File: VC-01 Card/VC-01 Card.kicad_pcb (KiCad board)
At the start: 2 copper layers, 55 x 41 mm, 60 parts, among them J1 AudioJack3, J2 Jack-DC, U1 ADS8681RUM, U2 TPS7A8801RTJT, U3 ADS8681RUM, U4 W25Q32JVSS, U5 LM1117-ADJ

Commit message: Added burden resistor jumper
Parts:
- added J3: BRDN, Connector_PinHeader_2.54mm:PinHeader_1x02_P2.54mm_Vertical, F.Cu at (150.7, 100.2)
- R1: footprint Resistor_SMD:R_2512_6332Metric -> Resistor_SMD:R_0805_2012Metric
- moved R1 10.8 mm to (144.8, 100.1), turned to 270 degrees
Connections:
- R1 pad 1: Net-(C2-Pad2) -> Net-(J3-Pad2)
- R1 pad 2: Net-(C2-Pad1) -> Net-(C2-Pad2)
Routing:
- net Net-(C2-Pad1): track 14.7 -> 7.66 mm
- net Net-(C2-Pad2): track 8.01 -> 13.4 mm
- net Net-(J3-Pad2): track 0.00 -> 3.79 mm
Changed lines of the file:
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@@
     (thickness 1.6)
     (drawings 55)
-    (tracks 497)
+    (tracks 498)
     (zones 0)
-    (modules 60)
-    (nets 41)
+    (modules 61)
+    (nets 42)
   )
   (page A4)
@@
   (net 39 /U1_GNDA)
   (net 40 /U3_GNDA)
+  (net 41 "Net-(J3-Pad2)")
   (net_class Default "This is the default net class."
     (clearance 0.2)
@@
     (add_net "Net-(J2-Pad1)")
     (add_net "Net-(J2-Pad2)")
+    (add_net "Net-(J3-Pad2)")
   )
   (net_class "Analog Path IC" ""
@@
     )
   )
-  (module Resistor_SMD:R_2512_6332Metric (layer F.Cu)
-    (at 147 110.7 180)
-    (descr "Resistor SMD 2512 (6332 Metric), square (rectangular) end terminal, IPC_7351 nominal, (Body size source: http://www.tortai-tech.com/upload/download/2011102023233369053.pdf), generated with kicad-footprint-generator")
-    (tags resistor)
-    (attr smd)
-    (fp_text reference R1 (at 0 -2.62) (layer F.SilkS)
-      (effects (font (size 1 1) (thickness 0.15)))
-    )
-    (fp_text value RB (at 0 2.62) (layer F.Fab)
-      (effects (font (size 1 1) (thickness 0.15)))
-    )
-    (fp_line (start -3.15 1.6) (end -3.15 -1.6) (layer F.Fab) (width 0.1))
-    (fp_line (start -3.15 -1.6) (end 3.15 -1.6) (layer F.Fab) (width 0.1))
-    (fp_line (start 3.15 -1.6) (end 3.15 1.6) (layer F.Fab) (width 0.1))
-    (fp_line (start 3.15 1.6) (end -3.15 1.6) (layer F.Fab) (width 0.1))
-    (fp_line (start -2.052064 -1.71) (end 2.052064 -1.71) (layer F.SilkS) (width 0.12))
-    (fp_line (start -2.052064 1.71) (end 2.052064 1.71) (layer F.SilkS) (width 0.12))
-    (fp_line (start -3.82 1.92) (end -3.82 -1.92) (layer F.CrtYd) (width 0.05))
-    (fp_line (start -3.82 -1.92) (end 3.82 -1.92) (layer F.CrtYd) (width 0.05))
-    (fp_line (start 3.82 -1.92) (end 3.82 1.92) (layer F.CrtYd) (width 0.05))
-    (fp_line (start 3.82 1.92) (end -3.82 1.92) (layer F.CrtYd) (width 0.05))
-    (fp_text user %R (at 0 0) (layer F.Fab)
-      (effects (font (size 1 1) (thickness 0.15)))
-    )
-    (pad 1 smd roundrect (at -2.9 0 180) (size 1.35 3.35) (layers F.Cu F.Paste F.Mask) (roundrect_rratio 0.185185)
-      (net 7 "Net-(C2-Pad2)"))
-    (pad 2 smd roundrect (at 2.9 0 180) (size 1.35 3.35) (layers F.Cu F.Paste F.Mask) (roundrect_rratio 0.185185)
-      (net 6 "Net-(C2-Pad1)"))
-    (model ${KISYS3DMOD}/Resistor_SMD.3dshapes/R_2512_6332Metric.wrl
-      (at (xyz 0 0 0))
-      (scale (xyz 1 1 1))
-      (rotate (xyz 0 0 0))
-    )
-  )
   (module Resistor_SMD:R_0603_1608Metric (layer F.Cu)
     (at 164.6 100.4)
@@
     )
   )
+  (module Resistor_SMD:R_0805_2012Metric (layer F.Cu)
+    (at 144.8 100.1 270)
+    (descr "Resistor SMD 0805 (2012 Metric), square (rectangular) end terminal, IPC_7351 nominal, (Body size source: https://docs.google.com/spreadsheets/d/1BsfQQcO9C6DZCsRaXUlFlo91Tg2WpOkGARC1WS5S8t0/edit?usp=sharing), generated with kicad-footprint-generator")
+    (tags resistor)
+    (attr smd)
+    (fp_text reference R1 (at 0 -1.65 90) (layer F.SilkS)
+      (effects (font (size 1 1) (thickness 0.15)))
+    )
+    (fp_text value RB (at 0 1.65 90) (layer F.Fab)
+      (effects (font (size 1 1) (thickness 0.15)))
+    )
+    (fp_line (start -1 0.6) (end -1 -0.6) (layer F.Fab) (width 0.1))
+    (fp_line (start -1 -0.6) (end 1 -0.6) (layer F.Fab) (width 0.1))
+    (fp_line (start 1 -0.6) (end 1 0.6) (layer F.Fab) (width 0.1))
+    (fp_line (start 1 0.6) (end -1 0.6) (layer F.Fab) (width 0.1))
+    (fp_line (start -0.258578 -0.71) (end 0.258578 -0.71) (layer F.SilkS) (width 0.12))
+    (fp_line (start -0.258578 0.71) (end 0.258578 0.71) (layer F.SilkS) (width 0.12))
+    (fp_line (start -1.68 0.95) (end -1.68 -0.95) (layer F.CrtYd) (width 0.05))
+    (fp_line (start -1.68 -0.95) (end 1.68 -0.95) (layer F.CrtYd) (width 0.05))
+    (fp_line (start 1.68 -0.95) (end 1.68 0.95) (layer F.CrtYd) (width 0.05))
+    (fp_line (start 1.68 0.95) (end -1.68 0.95) (layer F.CrtYd) (width 0.05))
+    (fp_text user %R (at 0 0 90) (layer F.Fab)
+      (effects (font (size 0.5 0.5) (thickness 0.08)))
+    )
+    (pad 1 smd roundrect (at -0.9375 0 270) (size 0.975 1.4) (layers F.Cu F.Paste F.Mask) (roundrect_rratio 0.25)
+      (net 41 "Net-(J3-Pad2)"))
+    (pad 2 smd roundrect (at 0.9375 0 270) (size 0.975 1.4) (layers F.Cu F.Paste F.Mask) (roundrect_rratio 0.25)
+      (net 7 "Net-(C2-Pad2)"))
+    (model ${KISYS3DMOD}/Resistor_SMD.3dshapes/R_0805_2012Metric.wrl
+      (at (xyz 0 0 0))
+      (scale (xyz 1 1 1))
+      (rotate (xyz 0 0 0))
+    )
+  )
+  (module Connector_PinHeader_2.54mm:PinHeader_1x02_P2.54mm_Vertical (layer F.Cu)
+    (at 150.7 100.2 270)
+    (descr "Through hole straight pin header, 1x02, 2.54mm pitch, single row")
+    (tags "Through hole pin header THT 1x02 2.54mm single row")
+    (fp_text reference J3 (at 0 -2.33 90) (layer F.SilkS)
+      (effects (font (size 1 1) (thickness 0.15)))
+    )
+    (fp_text value BRDN (at 0 4.87 90) (layer F.Fab)
+      (effects (font (size 1 1) (thickness 0.15)))
+    )
+    (fp_line (start -0.635 -1.27) (end 1.27 -1.27) (layer F.Fab) (width 0.1))
+    (fp_line (start 1.27 -1.27) (end 1.27 3.81) (layer F.Fab) (width 0.1))
+    (fp_line (start 1.27 3.81) (end -1.27 3.81) (layer F.Fab) (width 0.1))
+    (fp_line (start -1.27 3.81) (end -1.27 -0.635) (layer F.Fab) (width 0.1))
+    (fp_line (start -1.27 -0.635) (end -0.635 -1.27) (layer F.Fab) (width 0.1))
+    (fp_line (start -1.33 3.87) (end 1.33 3.87) (layer F.SilkS) (width 0.12))
+    (fp_line (start -1.33 1.27) (end -1.33 3.87) (layer F.SilkS) (width 0.12))
+    (fp_line (start 1.33 1.27) (end 1.33 3.87) (layer F.SilkS) (width 0.12))
+    (fp_line (start -1.33 1.27) (end 1.33 1.27) (layer F.SilkS) (width 0.12))
+    (fp_line (start -1.33 0) (end -1.33 -1.33) (layer F.SilkS) (width 0.12))
+    (fp_line (start -1.33 -1.33) (end 0 -1.33) (layer F.SilkS) (width 0.12))
+    (fp_line (start -1.8 -1.8) (end -1.8 4.35) (layer F.CrtYd) (width 0.05))
+    (fp_line (start -1.8 4.35) (end 1.8 4.35) (layer F.CrtYd) (width 0.05))
+    (fp_line (start 1.8 4.35) (end 1.8 -1.8) (layer F.CrtYd) (width 0.05))
+    (fp_line (start 1.8 -1.8) (end -1.8 -1.8) (layer F.CrtYd) (width 0.05))
+    (fp_text user %R (at 0 1.27) (layer F.Fab)
+      (effects (font (size 1 1) (thickness 0.15)))
+    )
+    (pad 1 thru_hole rect (at 0 0 270) (size 1.7 1.7) (drill 1) (layers *.Cu *.Mask)
+      (net 6 "Net-(C2-Pad1)"))
+    (pad 2 thru_hole oval (at 0 2.54 270) (size 1.7 1.7) (drill 1) (layers *.Cu *.Mask)
+      (net 41 "Net-(J3-Pad2)"))
+    (model ${KISYS3DMOD}/Connector_PinHeader_2.54mm.3dshapes/PinHeader_1x02_P2.54mm_Vertical.wrl
+      (at (xyz 0 0 0))
+      (scale (xyz 1 1 1))
+      (rotate (xyz 0 0 0))
+    )
+  )
   (gr_arc (start 177 100.2) (end 179 100.2) (angle -90) (layer Edge.Cuts) (width 0.05))
   (gr_arc (start 177 137.2) (end 177 139.2) (angle -90) (layer Edge.Cuts) (width 0.05))
@@
   (segment (start 153.985 104.93) (end 154.015 104.9) (width 0.4) (layer F.Cu) (net 6) (status 30))
   (segment (start 152.6 104.93) (end 153.985 104.93) (width 0.4) (layer F.Cu) (net 6) (status 30))
-  (segment (start 149.07 104.13) (end 150.65 104.13) (width 0.4) (layer F.Cu) (net 6))
-  (segment (start 148 105.2) (end 149.07 104.13) (width 0.4) (layer F.Cu) (net 6))
-  (segment (start 148 108.2) (end 148 105.2) (width 0.4) (layer F.Cu) (net 6))
-  (segment (start 144.1 110.7) (end 145.5 110.7) (width 0.4) (layer F.Cu) (net 6))
-  (segment (start 145.5 110.7) (end 148 108.2) (width 0.4) (layer F.Cu) (net 6))
+  (segment (start 150.7 104.08) (end 150.65 104.13) (width 0.4) (layer F.Cu) (net 6))
+  (segment (start 150.7 100.2) (end 150.7 104.08) (width 0.4) (layer F.Cu) (net 6))
   (segment (start 151.83 106.67) (end 152.6 105.9) (width 0.4) (layer F.Cu) (net 7) (status 20))
   (segment (start 150.65 106.67) (end 151.83 106.67) (width 0.4) (layer F.Cu) (net 7) (status 10))
   (segment (start 152.6 105.9) (end 154 105.9) (width 0.4) (layer F.Cu) (net 7) (status 30))
-  (segment (start 150.2 110.4) (end 149.9 110.7) (width 0.4) (layer F.Cu) (net 7))
-  (segment (start 150.65 106.67) (end 150.2 107.12) (width 0.4) (layer F.Cu) (net 7))
-  (segment (start 150.2 107.12) (end 150.2 110.4) (width 0.4) (layer F.Cu) (net 7))
+  (segment (start 148 105.4) (end 149.27 106.67) (width 0.4) (layer F.Cu) (net 7))
+  (segment (start 148 102.7) (end 148 105.4) (width 0.4) (layer F.Cu) (net 7))
+  (segment (start 149.27 106.67) (end 150.65 106.67) (width 0.4) (layer F.Cu) (net 7))
+  (segment (start 144.8 101.0375) (end 146.3375 101.0375) (width 0.4) (layer F.Cu) (net 7))
+  (segment (start 146.3375 101.0375) (end 148 102.7) (width 0.4) (layer F.Cu) (net 7))
   (segment (start 161.1625 124.325) (end 161.7 123.7875) (width 0.25) (layer F.Cu) (net 8) (status 20))
   (segment (start 160.1625 124.325) (end 161.1625 124.325) (width 0.25) (layer F.Cu) (net 8) (status 10))
@@
   (segment (start 160.1375 121.6) (end 160.1375 123.0625) (width 0.25) (layer F.Cu) (net 40) (status 10))
   (segment (start 160.1375 123.0625) (end 159.8625 123.3375) (width 0.25) (layer F.Cu) (net 40))
+  (segment (start 147.1225 99.1625) (end 148.16 100.2) (width 0.4) (layer F.Cu) (net 41))
+  (segment (start 144.8 99.1625) (end 147.1225 99.1625) (width 0.4) (layer F.Cu) (net 41))
   (zone (net 1) (net_name GND) (layer F.Cu) (hatch edge 0.508)
     (priority 1)

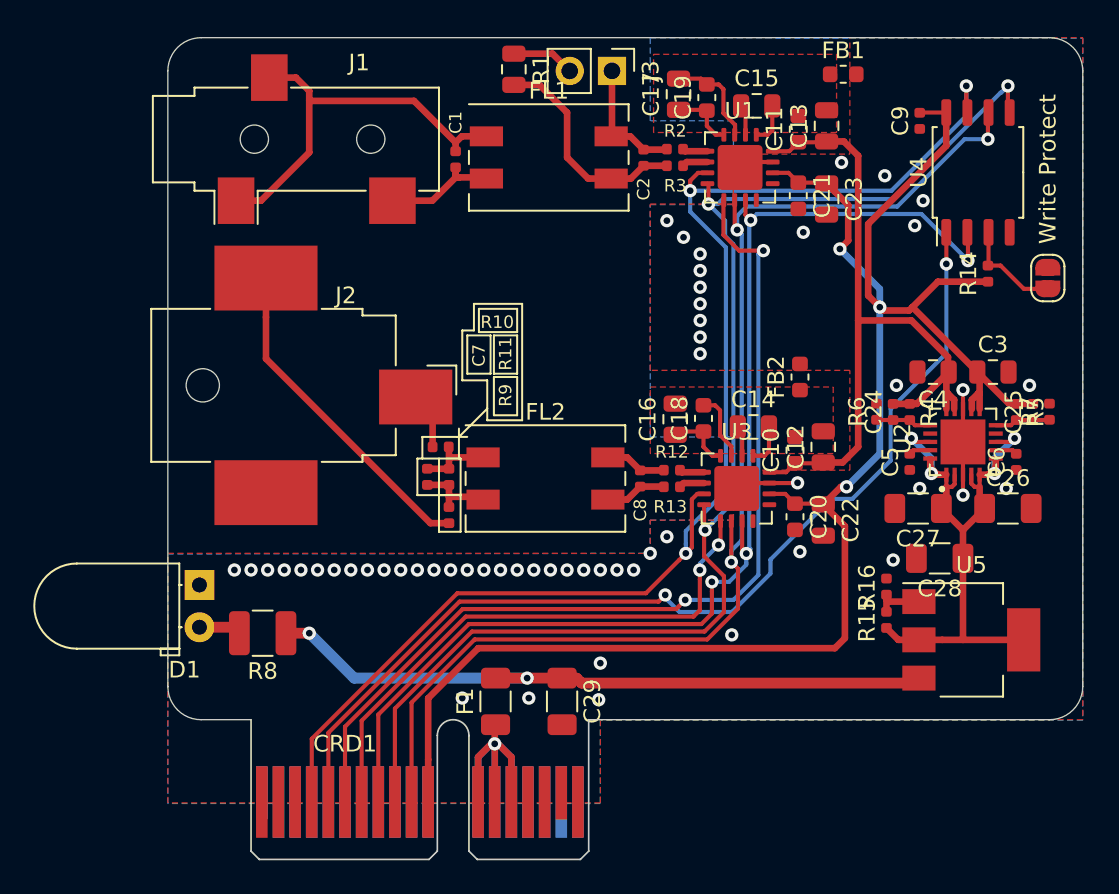
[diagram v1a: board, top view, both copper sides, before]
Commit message: Added value silkscreen to vc card
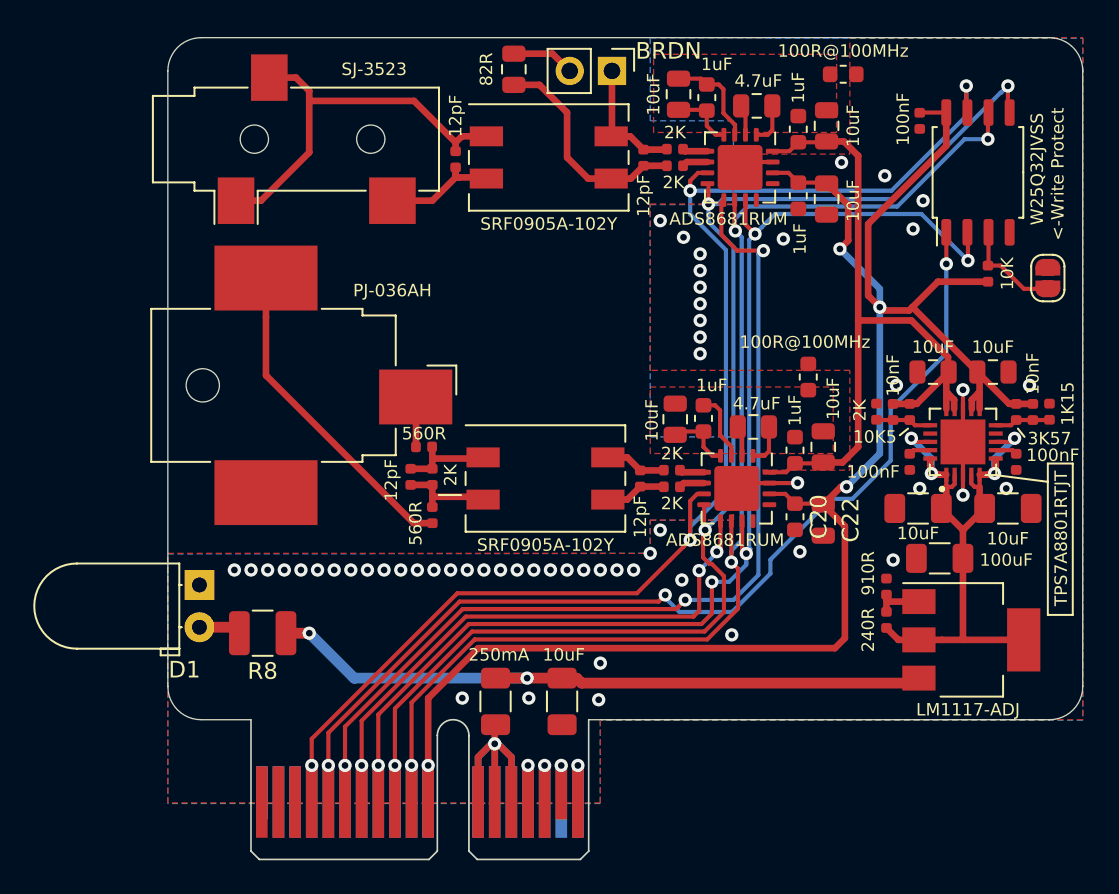
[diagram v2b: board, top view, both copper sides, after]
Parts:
- FB1, FB2: value Ferrite_Bead -> 100R@100MHz
- J1: value AudioJack3 -> SJ-3523
- J2: value Jack-DC -> PJ-036AH
- JP1: value Write Protect -> <-Write Protect
- R1: value RB -> 82R
- moved C7 1.00 mm to (138.6, 124.6)
- moved R10 1.00 mm to (139.4, 122.8)
- moved R11 1.00 mm to (139.9, 124.6)
- moved R9 1.00 mm to (139.9, 126.9)
- moved FB2 0.50 mm to (162.5, 118.6)
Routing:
- net GND: track 12.2 -> 29.3 mm, vias 55 -> 60
- net /SO: track 72.9 -> 75.4 mm, vias 4 -> 5
- net /~CS_CURRENT: track 57.7 -> 60.1 mm, vias 2 -> 3
- net /SI: track 79.6 -> 81.9 mm, vias 3 -> 4
- net /SCLK: track 75.0 -> 77.3 mm, vias 3 -> 4
- net +3V3: track 107.0 -> 109.2 mm, vias 3 -> 4
- net /~CS_FLASH: track 61.3 -> 63.5 mm, vias 2 -> 3
- net /~CS_VOLTAGE: track 35.1 -> 37.1 mm, vias 2 -> 3
- net Net-(J2-Pad1): track 3.42 -> 4.44 mm
- net Net-(C7-Pad2): track 4.75 -> 5.75 mm
- net Net-(C7-Pad1): track 4.70 -> 5.70 mm
- net /~RST: track 82.6 -> 83.6 mm, vias 3 -> 4
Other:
- net class Analog Path IC: clearance 0.25 -> 0.2

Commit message: Added BOM to VC-01 and tidied silkscreen, added thermistor to hat. Regenerated gerbers & PDFs
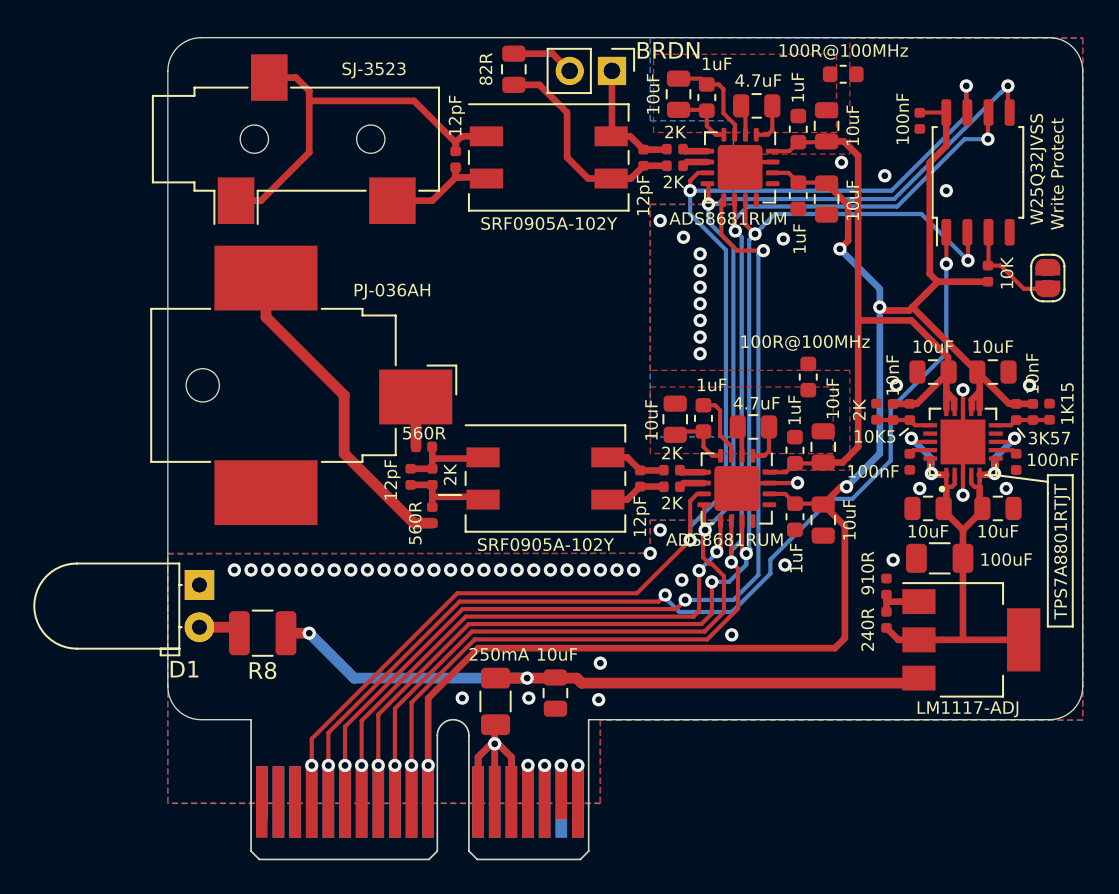
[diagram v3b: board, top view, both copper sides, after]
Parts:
- C26, C27, C29: footprint Capacitor_SMD:C_1206_3216Metric -> Capacitor_SMD:C_0805_2012Metric
- JP1: value <-Write Protect -> Write Protect
- moved C29 0.64 mm to (147.3, 137.6)
- moved C26 0.60 mm to (173.9, 126.5)
- moved C27 0.60 mm to (169.7, 126.5)
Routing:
- net +3V3: track 109.2 -> 106.0 mm
- net GND: vias 60 -> 59
